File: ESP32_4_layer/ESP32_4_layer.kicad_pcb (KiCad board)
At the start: 4 copper layers, 85 parts, among them J1 SS-52400-003, J2 JST_S2B-PH-K-S_LF__SN_, J3 GSD090012SEU_SDcard_Connector, J4 Conn_01x05_Pin, J5 Conn_01x04_Pin, Q1 TEMT6000X01, Q2 BC817, Q3 BC817, U1 MCP73871-4CC, U2 ESP32-C3-WROOM-02-H4, U3 CP2102N-Axx-xQFN20, U4 USBLC6-2SC6, U5 W25Q32JVSS, U6 BME280, U7 MAX4466EXK

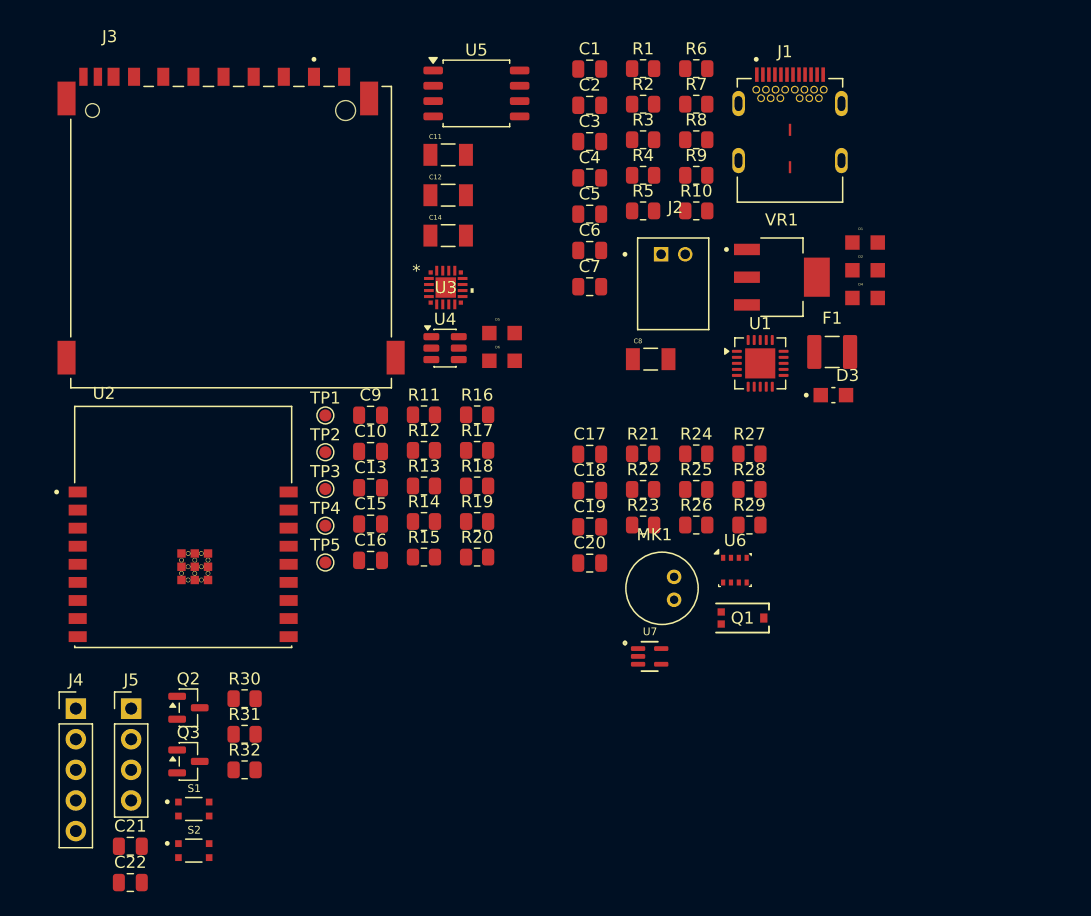
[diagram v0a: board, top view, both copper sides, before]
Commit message: upto inner layer copper zone
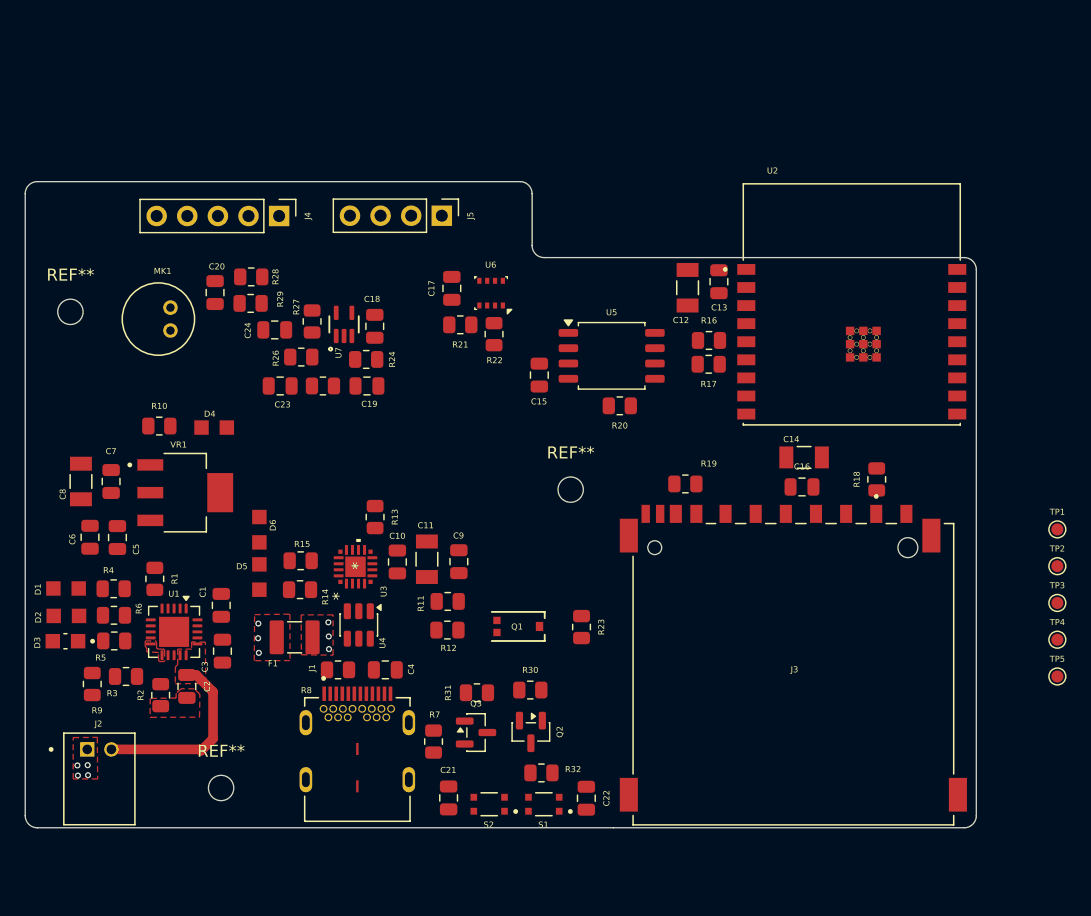
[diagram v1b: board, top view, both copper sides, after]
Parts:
- added C23: 1uf, Capacitor_SMD:C_0805_2012Metric, F.Cu at (121.9, 74.4)
- added C24: 10nf, Capacitor_SMD:C_0805_2012Metric, F.Cu at (121.5, 69.8)
- added REF**: MountingHole_2.1mm, MountingHole:MountingHole_2.1mm, F.Cu at (146.0, 83.0)
- added REF**: MountingHole_2.1mm, MountingHole:MountingHole_2.1mm, F.Cu at (104.5, 68.2)
- added REF**: MountingHole_2.1mm, MountingHole:MountingHole_2.1mm, F.Cu at (117.0, 107.8)
- moved D1 72.2 mm to (104.1, 91.2), turned to 180 degrees
- moved D2 72.2 mm to (104.2, 93.5), turned to 180 degrees
- moved D3 66.9 mm to (104.1, 95.6), turned to 180 degrees
- moved R6 66.3 mm to (108.1, 93.4), turned to 180 degrees
- moved R9 65.5 mm to (106.3, 99.1), turned to 90 degrees
- moved R2 63.3 mm to (112.0, 100.0), turned to 90 degrees
- moved J2 62.9 mm to (106.9, 107.0)
- moved J1 62.7 mm to (128.3, 107.1)
- moved R3 61.8 mm to (109.1, 98.5)
- moved TP1 61.5 mm to (186.4, 86.3)
- moved TP2 61.5 mm to (186.4, 89.3)
- moved TP3 61.5 mm to (186.4, 92.4)
- moved TP4 61.5 mm to (186.4, 95.5)
- moved TP5 61.5 mm to (186.4, 98.5)
- moved J3 59.1 mm to (164.5, 98.3)
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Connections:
- C19 pad 1: GND -> Net-(U7-IN-)
- MK1 pad OUT: Net-(U7-IN+) -> Net-(C24-Pad1)
- R24 pad 1: GND -> Net-(U7-IN-)
- R25 pad 1: GND -> Net-(U7-IN-)
- R25 pad 2: GND -> Net-(C23-Pad2)
- R26 pad 1: Net-(U7-IN+) -> /ESP32 C3 02/Sensors/IN+
- R27 pad 2: Net-(U7-IN+) -> /ESP32 C3 02/Sensors/IN+
- R29 pad 2: Net-(U7-IN+) -> Net-(C24-Pad1)
- U4 pad 1: /USB_DN -> /ESP32 C3 02/USB_D -
- U4 pad 3: /USB_DP -> /ESP32 C3 02/USB_D +
- U4 pad 4: /ESP32 C3 02/USB_D + -> /USB_DP
- U4 pad 6: /ESP32 C3 02/USB_D - -> /USB_DN
- U7 pad 1: Net-(U7-IN+) -> /ESP32 C3 02/Sensors/IN+
- U7 pad 3: GND -> Net-(U7-IN-)
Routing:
- net /VBAT: track 0.00 -> 15.5 mm
- net GND: vias 0 -> 4
- net /VBUS: vias 0 -> 3
- net /+5V_USB: vias 0 -> 3
- added copper zone on In1.Cu, net +3.3V
- added copper zone on F.Cu, net /+5V_USB
- added copper zone on In1.Cu, net /+5V_USB
- added copper zone on F.Cu, net /VBAT
- added copper zone on F.Cu, net /VBUS
- added copper zone on In1.Cu, net /VBUS
- added copper zone on F.Cu, net GND
- added copper zone on In2.Cu, net GND
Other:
- board outline added: 78.9 x 53.6 mm

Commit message: Routing finished_1
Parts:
- moved TP4 47.6 mm to (145.3, 71.3)
- moved TP1 39.2 mm to (147.2, 84.5)
- moved TP3 38.5 mm to (152.8, 73.6)
- moved TP2 31.5 mm to (157.4, 76.9)
- moved R23 24.2 mm to (128.3, 79.0), turned to 90 degrees
- moved TP5 18.2 mm to (178.0, 82.3)
- moved Q1 18.0 mm to (132.1, 79.0)
- moved R22 6.51 mm to (135.7, 64.9), turned to 180 degrees
- moved R19 6.23 mm to (149.3, 82.4)
- moved REF** 6.00 mm to (143.1, 88.2)
- moved R21 5.88 mm to (140.1, 64.4), turned to 90 degrees
- moved R20 5.38 mm to (146.3, 79.9)
- moved U5 5.34 mm to (145.7, 75.7)
- moved C15 4.99 mm to (139.8, 76.9)
- moved C18 4.87 mm to (126.4, 65.9), turned to 0 degrees
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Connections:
- J5 pad 2: /ESP32 C3 02/SDA -> /ESP32 C3 02/SCL
- J5 pad 3: /ESP32 C3 02/SCL -> /ESP32 C3 02/SDA
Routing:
- net GND: track 0.00 -> 196.9 mm, vias 4 -> 30
- net +3.3V: track 0.00 -> 89.1 mm, vias 0 -> 23
- net /ESP32 C3 02/EN: track 0.00 -> 87.6 mm, vias 0 -> 2
- net /ESP32 C3 02/GPIO19: track 0.00 -> 70.0 mm, vias 0 -> 2
- net /ESP32 C3 02/GPIO18: track 0.00 -> 67.4 mm, vias 0 -> 2
- net /ESP32 C3 02/BOOT: track 0.00 -> 67.3 mm, vias 0 -> 2
- net /ESP32 C3 02/MISO_DO: track 0.00 -> 65.7 mm
- net /ESP32 C3 02/TX_RX: track 0.00 -> 63.9 mm, vias 0 -> 2
- net /ESP32 C3 02/RX_TX: track 0.00 -> 61.9 mm, vias 0 -> 2
- net /ESP32 C3 02/PHOTO_C: track 0.00 -> 59.3 mm, vias 0 -> 2
- net /ESP32 C3 02/MOSI_DI: track 0.00 -> 55.5 mm
- net /ESP32 C3 02/SCL: track 0.00 -> 53.1 mm, vias 0 -> 2
- net /ESP32 C3 02/SDA: track 0.00 -> 50.9 mm, vias 0 -> 2
- net /ESP32 C3 02/GPIO8: track 0.00 -> 48.8 mm, vias 0 -> 2
- net /ESP32 C3 02/MIC_OUT: track 0.00 -> 41.0 mm, vias 0 -> 2
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- added copper zone on F.Cu, net +3.3V
- added copper zone on F.Cu, net +5V
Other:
- board size 78.9 x 53.6 mm -> 81.1 x 53.6 mm

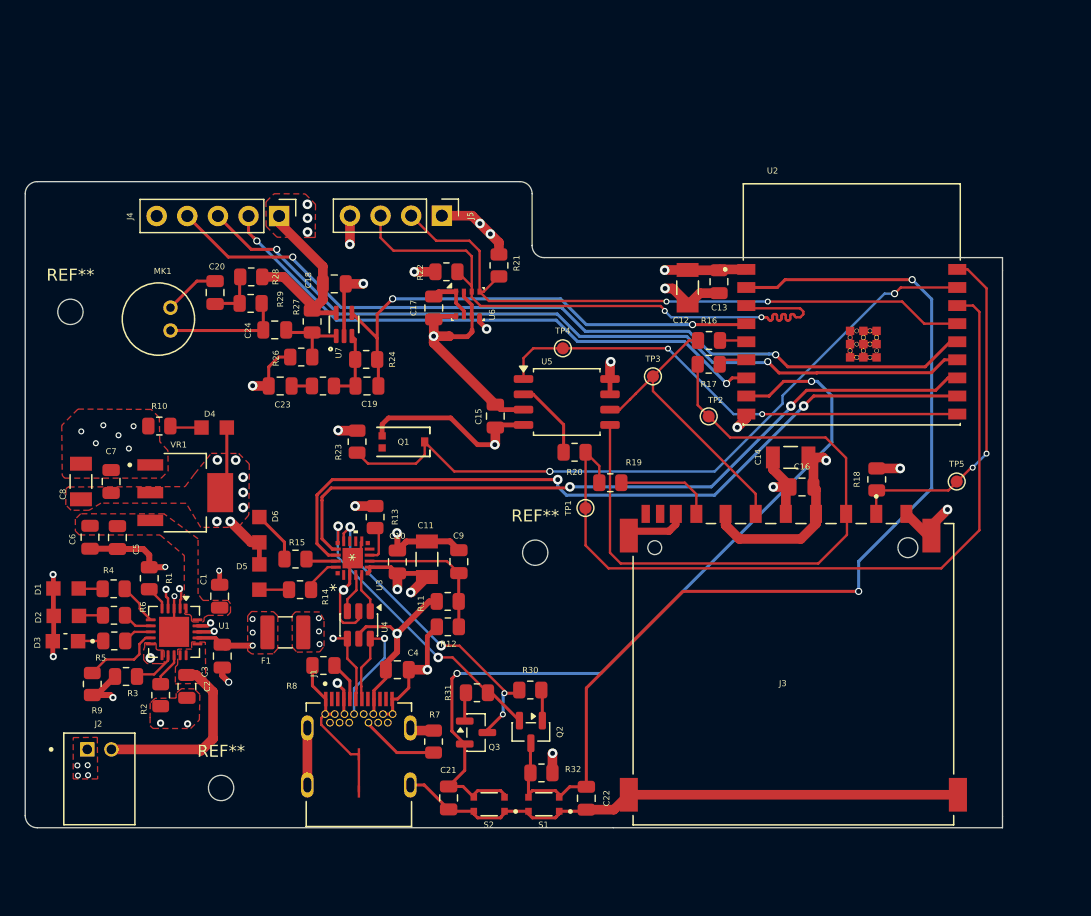
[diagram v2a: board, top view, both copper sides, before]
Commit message: pcb completed upto dfm check
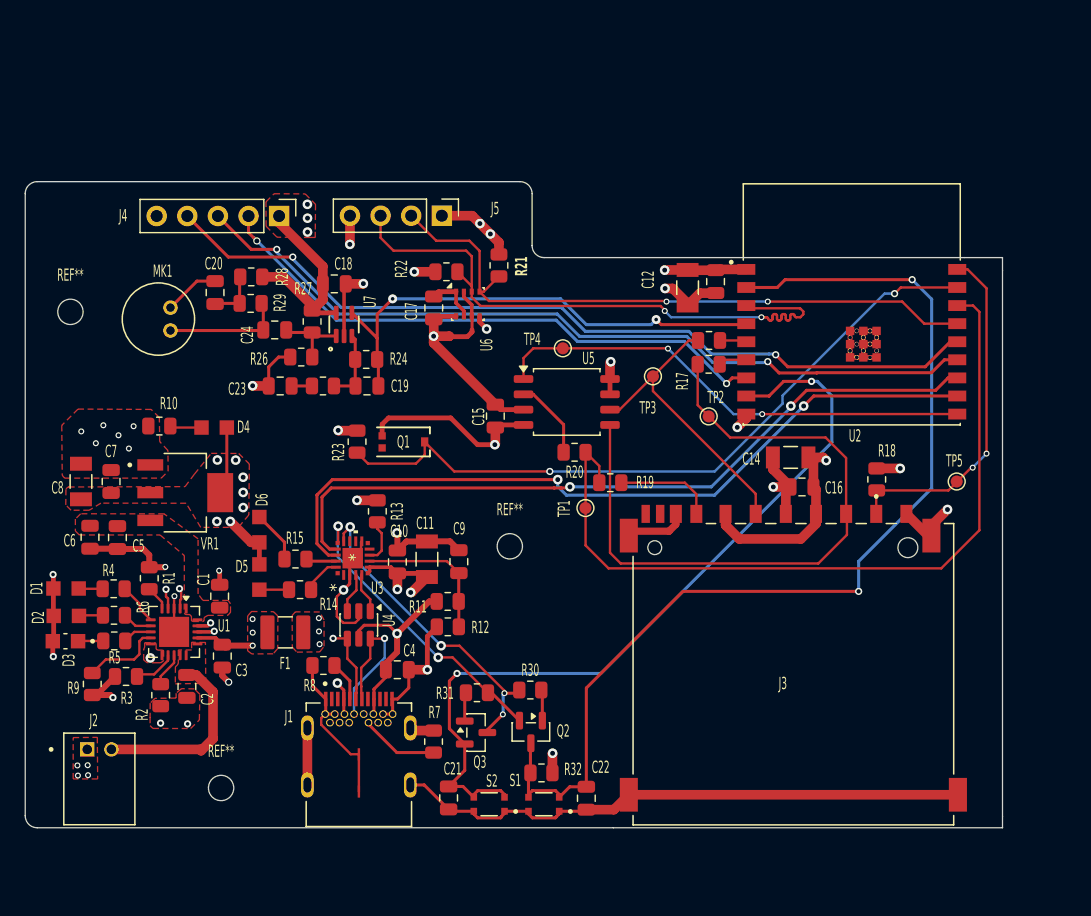
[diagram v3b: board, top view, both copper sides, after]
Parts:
- moved REF** 2.18 mm to (140.9, 87.7)
- moved R13 0.51 mm to (130.0, 84.8)
- moved C13 0.28 mm to (158.0, 65.7)
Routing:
- net Net-(U3-~{RST}): track 3.06 -> 3.66 mm
